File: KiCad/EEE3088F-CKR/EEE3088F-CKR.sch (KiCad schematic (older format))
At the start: 0 parts

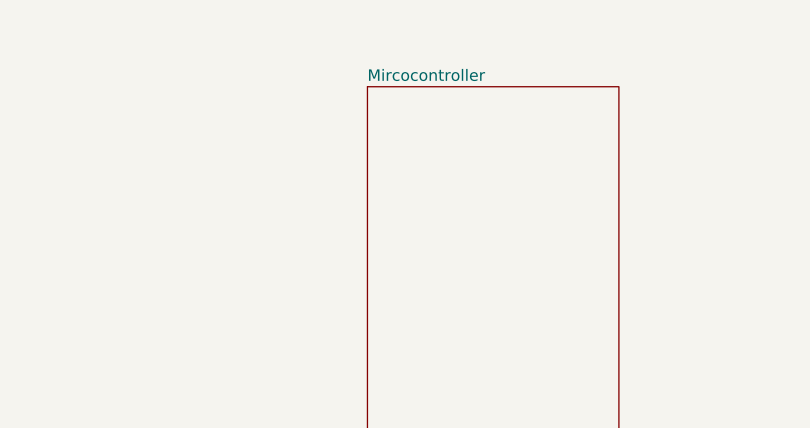
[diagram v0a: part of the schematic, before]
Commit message: microcontroller added
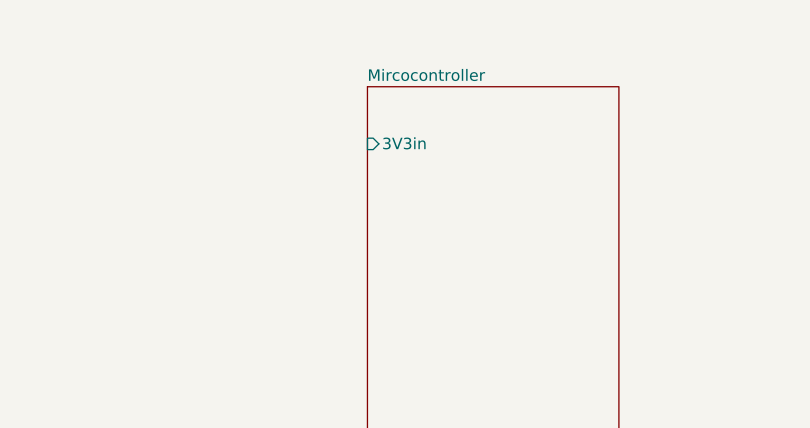
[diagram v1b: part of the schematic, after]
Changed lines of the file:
@@
 F0 "Mircocontroller" 50
 F1 "Mircocontroller.sch" 50
+F2 "3V3in" I L 5500 1750 50
 $EndSheet
 $Sheet
